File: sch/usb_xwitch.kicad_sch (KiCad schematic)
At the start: 42 parts

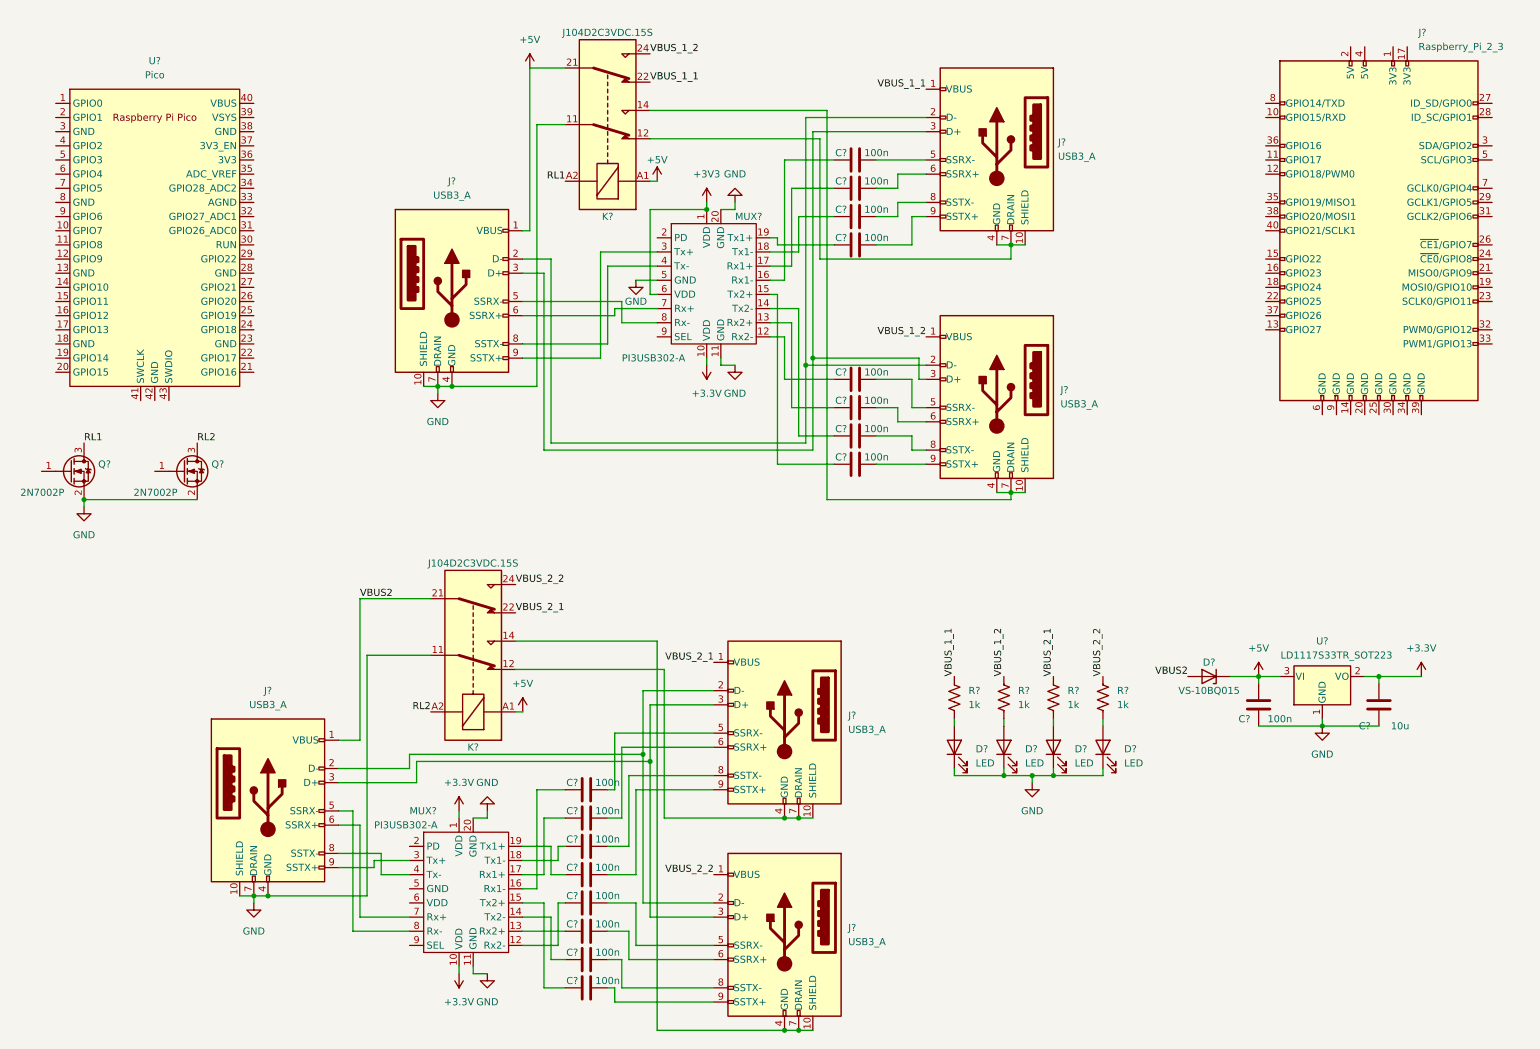
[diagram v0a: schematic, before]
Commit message: updated schematics
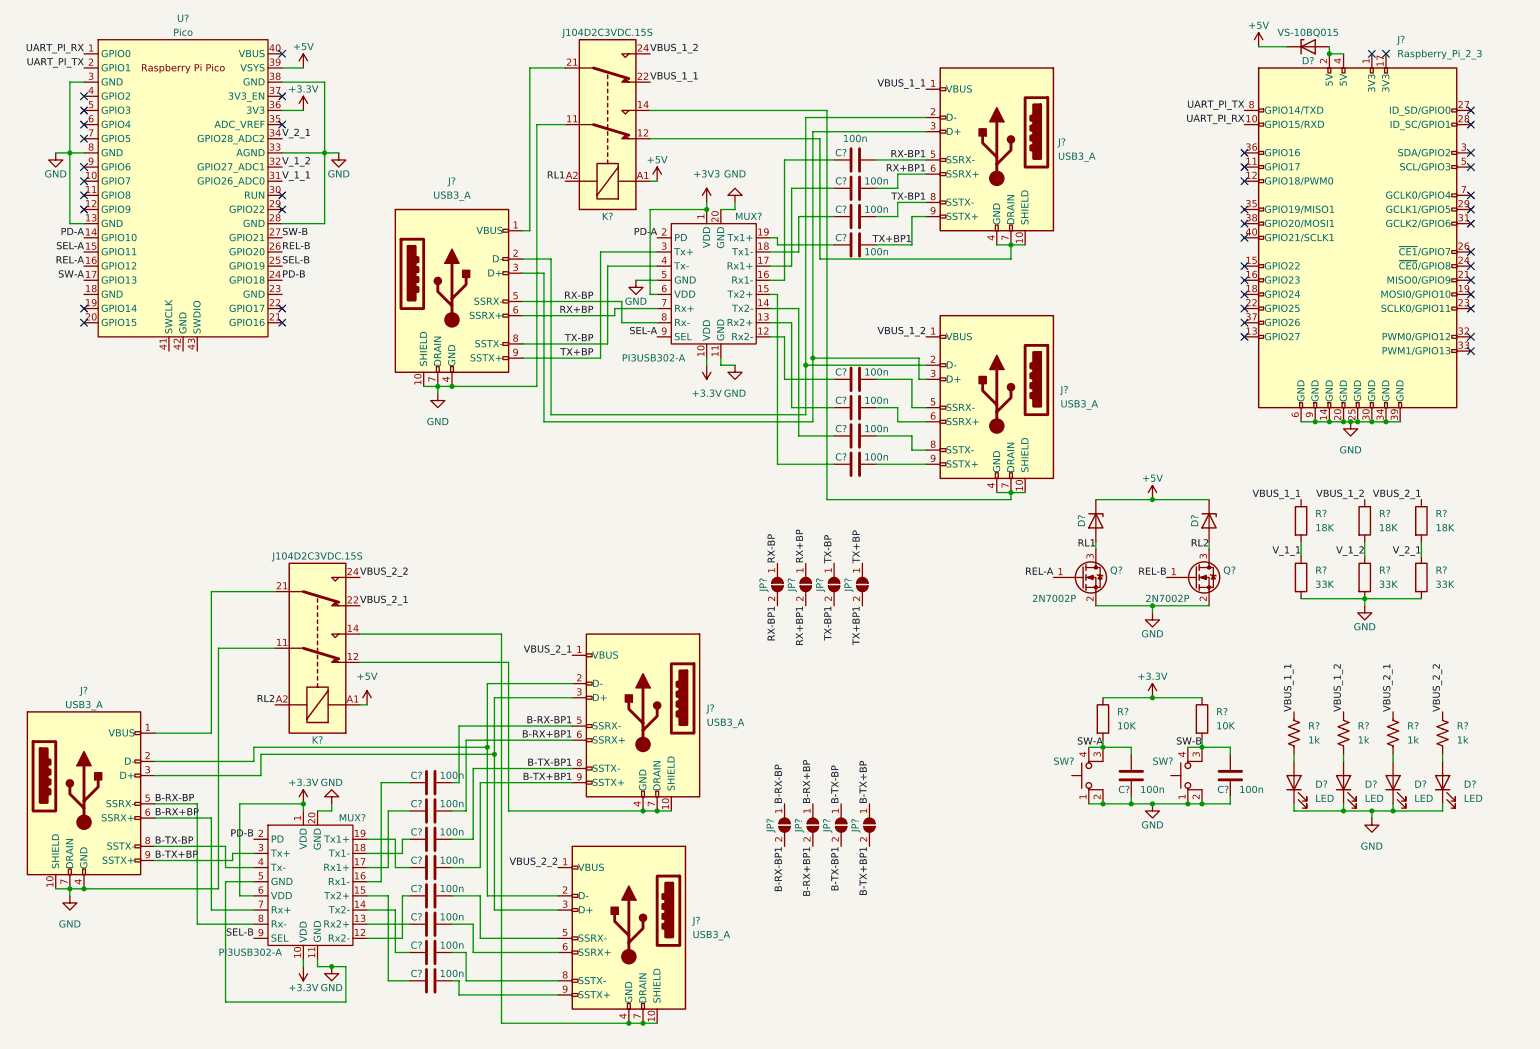
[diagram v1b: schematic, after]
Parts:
- removed C?: 10u, Capacitor_SMD:C_1206_3216Metric_Pad1.33x1.80mm_HandSolder, symbol Device:C
- removed C?: 100n, Capacitor_SMD:C_1206_3216Metric_Pad1.33x1.80mm_HandSolder, symbol Device:C
- removed D?: VS-10BQ015, Diode_SMD:D_SMB_Handsoldering, symbol Diode:Z2SMBxxx
- removed U?: LD1117S33TR_SOT223, Package_TO_SOT_SMD:SOT-223-3_TabPin2, symbol Regulator_Linear:LD1117S33TR_SOT223
- added C? (x2): 100n, Capacitor_SMD:C_1206_3216Metric_Pad1.33x1.80mm_HandSolder, symbol Device:C
- added D? (x3): VS-10BQ015, Diode_SMD:D_SMB_Handsoldering, symbol Diode:Z2SMBxxx
- added JP? (x8): SolderJumper_2_Open, Jumper:SolderJumper-2_P1.3mm_Open_RoundedPad1.0x1.5mm, symbol Jumper:SolderJumper_2_Open
- added R? (x2): 10K, Resistor_SMD:R_0603_1608Metric_Pad0.98x0.95mm_HandSolder, symbol Device:R
- added R? (x3): 18K, Resistor_SMD:R_0805_2012Metric_Pad1.20x1.40mm_HandSolder, symbol Device:R
- added R? (x3): 33K, Resistor_SMD:R_0805_2012Metric_Pad1.20x1.40mm_HandSolder, symbol Device:R
- added SW? (x2): SW_MEC_5E, symbol Switch:SW_MEC_5E
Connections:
- net +3V3: now also MUX?.6 (VDD), U?.36 (3V3), R?.1, R?.1
- net +5V: now also U?.39 (VSYS), D?.1 (K), D?.1 (K), D?.1 (K); no longer J?.1 (VBUS), K?.21
- net GND: now also J?.14 (GND), J?.20 (GND), J?.25 (GND), J?.30 (GND), J?.34 (GND), J?.39 (GND), J?.6 (GND), J?.9 (GND), MUX?.5 (GND), U?.13 (GND), U?.28 (GND), U?.3 (GND), U?.33 (AGND), U?.38 (GND), U?.8 (GND), C?.1, C?.1, R?.2, R?.2, R?.2, SW?.1, SW?.1, SW?.2, SW?.2
- net RL1: now also D?.2 (A)
- net RL2: now also D?.2 (A)
- net VBUS_1_1: now also R?.1
- net VBUS_1_2: now also R?.1
- net VBUS_2_1: now also R?.1
- net REL-A: now reaches Q?.1 (G)
- net REL-A: now also U?.16 (GPIO12)
- net B-RX-BP1: now reaches C?.2, J?.5 (SSRX-)
- net B-RX-BP1: now also JP?.2 (B)
- net B-RX+BP1: now reaches C?.2, J?.6 (SSRX+)
- net B-RX+BP1: now also JP?.2 (B)
- net B-TX-BP1: now reaches C?.2, J?.8 (SSTX-)
- net B-TX-BP1: now also JP?.2 (B)
- net B-TX+BP1: now reaches C?.2, J?.9 (SSTX+)
- net B-TX+BP1: now also JP?.2 (B)
- net PD-B: now reaches MUX?.2 (PD)
- net PD-B: now also U?.24 (GPIO18)
- net B-TX+BP: now reaches J?.9 (SSTX+), MUX?.3 (Tx+)
- net B-TX+BP: now also JP?.1 (A)
- net B-TX-BP: now reaches J?.8 (SSTX-), MUX?.4 (Tx-)
- net B-TX-BP: now also JP?.1 (A)
- net B-RX+BP: now reaches J?.6 (SSRX+), MUX?.7 (Rx+)
- net B-RX+BP: now also JP?.1 (A)
- net B-RX-BP: now reaches J?.5 (SSRX-), MUX?.8 (Rx-)
- net B-RX-BP: now also JP?.1 (A)
- net SEL-B: now reaches MUX?.9 (SEL)
- net SEL-B: now also U?.25 (GPIO19)
- net PD-A: now reaches MUX?.2 (PD)
- net PD-A: now also U?.14 (GPIO10)
- net TX+BP: now reaches J?.9 (SSTX+), MUX?.3 (Tx+)
- net TX+BP: now also JP?.1 (A)
- net TX-BP: now reaches J?.8 (SSTX-), MUX?.4 (Tx-)
- net TX-BP: now also JP?.1 (A)
- net RX+BP: now reaches J?.6 (SSRX+), MUX?.7 (Rx+)
- net RX+BP: now also JP?.1 (A)
- net RX-BP: now reaches J?.5 (SSRX-), MUX?.8 (Rx-)
- net RX-BP: now also JP?.1 (A)
- net SEL-A: now reaches MUX?.9 (SEL)
- net SEL-A: now also U?.15 (GPIO11)
- net REL-B: now reaches Q?.1 (G)
- net REL-B: now also U?.26 (GPIO20)
- net RX-BP1: now reaches C?.2, J?.5 (SSRX-)
- net RX-BP1: now also JP?.2 (B)
- net RX+BP1: now reaches C?.2, J?.6 (SSRX+)
- net RX+BP1: now also JP?.2 (B)
- net TX-BP1: now reaches C?.2, J?.8 (SSTX-)
- net TX-BP1: now also JP?.2 (B)
- net TX+BP1: now reaches C?.2, J?.9 (SSTX+)
- net TX+BP1: now also JP?.2 (B)
- net UART_PI_RX: now reaches U?.1 (GPIO0)
- net UART_PI_RX: now also J?.10 (GPIO15/RXD)
- net SW-A: now reaches U?.17 (GPIO13)
- net SW-A: now also C?.2, R?.2, SW?.3 (K), SW?.4 (A)
- net UART_PI_TX: now reaches U?.2 (GPIO1)
- net UART_PI_TX: now also J?.8 (GPIO14/TXD)
- net SW-B: now reaches U?.27 (GPIO21)
- net SW-B: now also C?.2, R?.2, SW?.3 (K), SW?.4 (A)
- net V_1_1: now reaches U?.31 (GPIO26_ADC0)
- net V_1_1: now also R?.1, R?.2
- net V_1_2: now reaches U?.32 (GPIO27_ADC1)
- net V_1_2: now also R?.1, R?.2
- net V_2_1: now reaches U?.34 (GPIO28_ADC2)
- net V_2_1: now also R?.1, R?.2
- net at J?.2 (5V): now also J?.4 (5V), D?.2 (A)
- net VBUS2: no longer names the net of J?.1 (VBUS), K?.21
- new net: J?.1 (VBUS), K?.21
- no-connect marks 0 -> 45
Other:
- moved on the sheet: C?, D?, J?, K?, MUX?, Q?, R?, U?

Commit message: add tp; ERC check
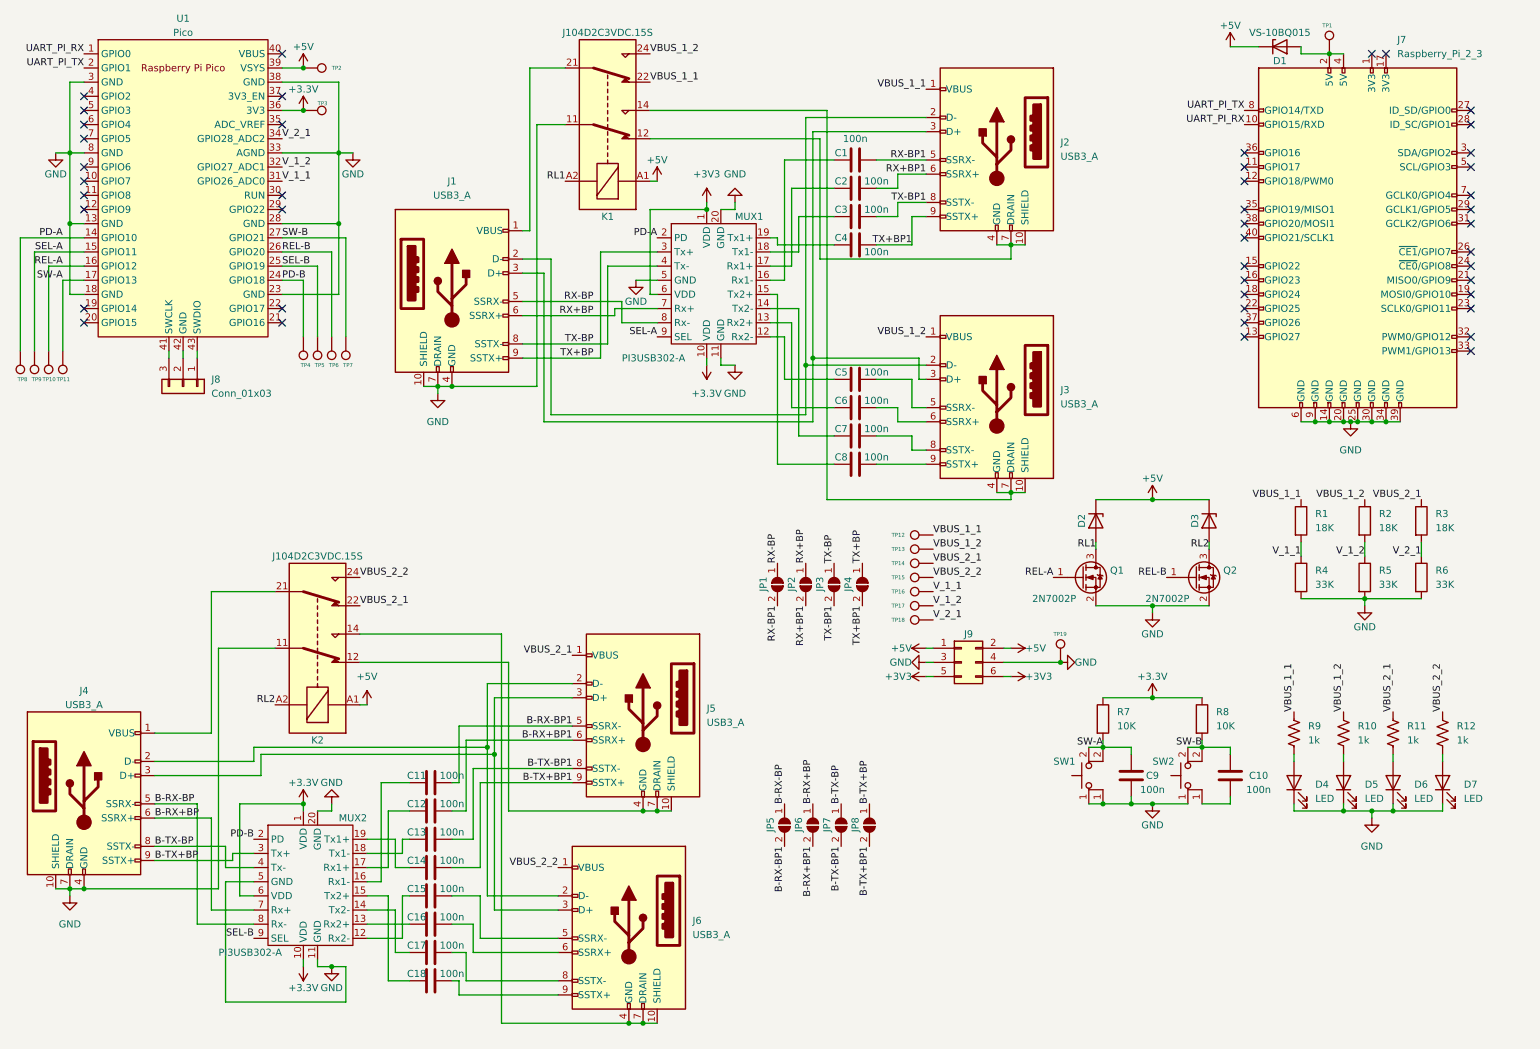
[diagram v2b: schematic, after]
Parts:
- removed SW?: SW_MEC_5E, symbol Switch:SW_MEC_5E
- added J8: Conn_01x03, Connector_PinHeader_2.00mm:PinHeader_1x03_P2.00mm_Vertical, symbol Connector_Generic:Conn_01x03
- added J9: Conn_02x03_Odd_Even, Connector_PinHeader_2.00mm:PinHeader_2x03_P2.00mm_Vertical, symbol Connector_Generic:Conn_02x03_Odd_Even
- added SW2: SW_MEC_5E, Button_Switch_THT:SW_PUSH-12mm, symbol Switch:SW_MEC_5E
- added TP1, TP10, TP11, TP12, TP13, TP14, TP15, TP16, TP17, TP18, TP19, TP2, TP3, TP4, TP5, TP6, TP7, TP8, TP9: TestPoint, TestPoint:TestPoint_Pad_D1.5mm, symbol Connector:TestPoint
- SW1: renamed from SW?; footprint (none) -> Button_Switch_THT:SW_PUSH-12mm
- gave numbers to parts that had none: 59
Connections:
- net +3V3: now also J9.5 (Pin_5), J9.6 (Pin_6), TP3.1
- net +5V: now also J9.1 (Pin_1), J9.2 (Pin_2), TP2.1
- net GND: now also U1.18 (GND), U1.23 (GND), J9.3 (Pin_3), J9.4 (Pin_4), SW2.1, TP19.1; no longer C10.1, SW1.2
- net PD-A: now also TP8.1
- net PD-B: now also TP4.1
- net REL-A: now also TP10.1
- net REL-B: now also TP6.1
- net SEL-A: now also TP9.1
- net SEL-B: now also TP5.1
- net SW-A: now also SW1.2, TP11.1; no longer SW1.3 (K), SW1.4 (A)
- net SW-B: now also SW2.2, TP7.1
- net VBUS_1_1: now also TP12.1
- net VBUS_1_2: now also TP13.1
- net VBUS_2_1: now also TP14.1
- net VBUS_2_2: now also TP15.1
- net V_1_1: now also TP16.1
- net V_1_2: now also TP17.1
- net V_2_1: now also TP18.1
- net at D1.2 (A), J7.2 (5V), J7.4 (5V): now also TP1.1
- net at U1.41 (SWCLK): now also J8.3 (Pin_3)
- net at U1.42 (GND): now also J8.2 (Pin_2)
- net at U1.43 (SWDIO): now also J8.1 (Pin_1)
- new net: C10.1, SW2.1
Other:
- moved on the sheet: D1

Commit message: updated lib using those in this repo
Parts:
- J1, J2, J3, J4, J5, J6: footprint USB3_A_AdamTech_USB-A3-S-RA:USB3_A_AdamTech_USB-A3-S-RA -> usb_xwitch:USB3_A_AdamTech_USB-A3-S-RA
- K1, K2: footprint Relay_THT:Relay_DPDT_Finder_30.22 -> usb_xwitch:J104D2C3VDC.15S
- MUX1, MUX2: symbol USB_MUX_DEMUX_PI3USB302-A:PI3USB302-A -> usb_xwitch:PI3USB302-A
- U1: symbol MCU_RaspberryPi_and_Boards:Pico -> usb_xwitch:Pico
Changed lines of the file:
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@@
     (property "Reference" "K2" (id 0) (at 67.31 143.51 90))
     (property "Value" "J104D2C3VDC.15S" (id 1) (at 67.31 110.49 90))
-    (property "Footprint" "Relay_THT:Relay_DPDT_Finder_30.22" (id 2) (at 66.548 92.71 0)
+    (property "Footprint" "usb_xwitch:J104D2C3VDC.15S" (id 2) (at 66.548 92.71 0)
       (effects (font (size 1.27 1.27)) hide)
     )
@@
       (effects (font (size 1.27 1.27)) (justify right))
     )
-    (property "Footprint" "USB3_A_AdamTech_USB-A3-S-RA:USB3_A_AdamTech_USB-A3-S-RA" (id 2) (at 185.42 78.74 0)
+    (property "Footprint" "usb_xwitch:USB3_A_AdamTech_USB-A3-S-RA" (id 2) (at 185.42 78.74 0)
       (effects (font (size 1.27 1.27)) hide)
     )
@@
       (effects (font (size 1.27 1.27)) (justify right))
     )
-    (property "Footprint" "USB3_A_AdamTech_USB-A3-S-RA:USB3_A_AdamTech_USB-A3-S-RA" (id 2) (at 121.92 135.89 0)
+    (property "Footprint" "usb_xwitch:USB3_A_AdamTech_USB-A3-S-RA" (id 2) (at 121.92 135.89 0)
       (effects (font (size 1.27 1.27)) hide)
     )
@@
     (pin "9")
   )
-  (symbol (lib_id "USB_MUX_DEMUX_PI3USB302-A:PI3USB302-A") (at 66.04 170.18 0) (unit 1)
+  (symbol (lib_id "usb_xwitch:PI3USB302-A") (at 66.04 170.18 0) (unit 1)
     (in_bom yes) (on_board yes)
     (property "Reference" "MUX2" (id 0) (at 71.12 157.48 0)
@@
     (pin "1")
   )
-  (symbol (lib_id "USB_MUX_DEMUX_PI3USB302-A:PI3USB302-A") (at 138.43 62.23 0) (unit 1)
+  (symbol (lib_id "usb_xwitch:PI3USB302-A") (at 138.43 62.23 0) (unit 1)
     (in_bom yes) (on_board yes)
     (property "Reference" "MUX1" (id 0) (at 142.24 49.53 0)
@@
       (effects (font (size 1.27 1.27)) (justify right))
     )
-    (property "Footprint" "USB3_A_AdamTech_USB-A3-S-RA:USB3_A_AdamTech_USB-A3-S-RA" (id 2) (at 119.38 173.99 0)
+    (property "Footprint" "usb_xwitch:USB3_A_AdamTech_USB-A3-S-RA" (id 2) (at 119.38 173.99 0)
       (effects (font (size 1.27 1.27)) hide)
     )
@@
     (property "Reference" "J4" (id 0) (at 25.4 134.62 0))
     (property "Value" "USB3_A" (id 1) (at 25.4 137.16 0))
-    (property "Footprint" "USB3_A_AdamTech_USB-A3-S-RA:USB3_A_AdamTech_USB-A3-S-RA" (id 2) (at 29.21 149.86 0)
+    (property "Footprint" "usb_xwitch:USB3_A_AdamTech_USB-A3-S-RA" (id 2) (at 29.21 149.86 0)
       (effects (font (size 1.27 1.27)) hide)
     )
@@
     (property "Reference" "J1" (id 0) (at 91.44 43.18 0))
     (property "Value" "USB3_A" (id 1) (at 91.44 45.72 0))
-    (property "Footprint" "USB3_A_AdamTech_USB-A3-S-RA:USB3_A_AdamTech_USB-A3-S-RA" (id 2) (at 95.25 59.69 0)
+    (property "Footprint" "usb_xwitch:USB3_A_AdamTech_USB-A3-S-RA" (id 2) (at 95.25 59.69 0)
       (effects (font (size 1.27 1.27)) hide)
     )
@@
       (effects (font (size 1.27 1.27)) (justify right))
     )
-    (property "Footprint" "USB3_A_AdamTech_USB-A3-S-RA:USB3_A_AdamTech_USB-A3-S-RA" (id 2) (at 185.42 34.29 0)
+    (property "Footprint" "usb_xwitch:USB3_A_AdamTech_USB-A3-S-RA" (id 2) (at 185.42 34.29 0)
       (effects (font (size 1.27 1.27)) hide)
     )
@@
     (property "Reference" "K1" (id 0) (at 119.38 49.53 90))
     (property "Value" "J104D2C3VDC.15S" (id 1) (at 119.38 16.51 90))
-    (property "Footprint" "Relay_THT:Relay_DPDT_Finder_30.22" (id 2) (at 118.618 -1.27 0)
+    (property "Footprint" "usb_xwitch:J104D2C3VDC.15S" (id 2) (at 118.618 -1.27 0)
       (effects (font (size 1.27 1.27)) hide)
     )
@@
     (pin "1")
   )
-  (symbol (lib_id "MCU_RaspberryPi_and_Boards:Pico") (at 43.18 44.45 0) (unit 1)
+  (symbol (lib_id "usb_xwitch:Pico") (at 43.18 44.45 0) (unit 1)
     (in_bom yes) (on_board yes)
     (property "Reference" "U1" (id 0) (at 43.18 13.97 0))
@@
     )
     (path "/8631f63c-abc2-47db-96b3-ee2fd07e9d0a"
-      (reference "J1") (unit 1) (value "USB3_A") (footprint "USB3_A_AdamTech_USB-A3-S-RA:USB3_A_AdamTech_USB-A3-S-RA")
+      (reference "J1") (unit 1) (value "USB3_A") (footprint "usb_xwitch:USB3_A_AdamTech_USB-A3-S-RA")
     )
     (path "/9118b6c6-d9a2-47dd-aea5-27a2b79677e2"
-      (reference "J2") (unit 1) (value "USB3_A") (footprint "USB3_A_AdamTech_USB-A3-S-RA:USB3_A_AdamTech_USB-A3-S-RA")
+      (reference "J2") (unit 1) (value "USB3_A") (footprint "usb_xwitch:USB3_A_AdamTech_USB-A3-S-RA")
     )
     (path "/17ca6d2b-651b-475e-9133-2f1f98ecc630"
-      (reference "J3") (unit 1) (value "USB3_A") (footprint "USB3_A_AdamTech_USB-A3-S-RA:USB3_A_AdamTech_USB-A3-S-RA")
+      (reference "J3") (unit 1) (value "USB3_A") (footprint "usb_xwitch:USB3_A_AdamTech_USB-A3-S-RA")
     )
     (path "/7777c39f-7409-4ac6-aa45-921399788f7d"
-      (reference "J4") (unit 1) (value "USB3_A") (footprint "USB3_A_AdamTech_USB-A3-S-RA:USB3_A_AdamTech_USB-A3-S-RA")
+      (reference "J4") (unit 1) (value "USB3_A") (footprint "usb_xwitch:USB3_A_AdamTech_USB-A3-S-RA")
     )
     (path "/32613975-ea2d-458f-a092-8f2ed600fa0e"
-      (reference "J5") (unit 1) (value "USB3_A") (footprint "USB3_A_AdamTech_USB-A3-S-RA:USB3_A_AdamTech_USB-A3-S-RA")
+      (reference "J5") (unit 1) (value "USB3_A") (footprint "usb_xwitch:USB3_A_AdamTech_USB-A3-S-RA")
     )
     (path "/734cb3cf-5e33-4360-8951-f60daf4bf50c"
-      (reference "J6") (unit 1) (value "USB3_A") (footprint "USB3_A_AdamTech_USB-A3-S-RA:USB3_A_AdamTech_USB-A3-S-RA")
+      (reference "J6") (unit 1) (value "USB3_A") (footprint "usb_xwitch:USB3_A_AdamTech_USB-A3-S-RA")
     )
     (path "/eeb933f2-c08b-4d89-bcac-799c4990513e"
@@
     )
     (path "/a781a132-2044-4d8e-a231-2f6e7cadcd25"
-      (reference "K1") (unit 1) (value "J104D2C3VDC.15S") (footprint "Relay_THT:Relay_DPDT_Finder_30.22")
+      (reference "K1") (unit 1) (value "J104D2C3VDC.15S") (footprint "usb_xwitch:J104D2C3VDC.15S")
     )
     (path "/0736d952-e7d6-49f7-9fe4-a9d4b55253bf"
-      (reference "K2") (unit 1) (value "J104D2C3VDC.15S") (footprint "Relay_THT:Relay_DPDT_Finder_30.22")
+      (reference "K2") (unit 1) (value "J104D2C3VDC.15S") (footprint "usb_xwitch:J104D2C3VDC.15S")
     )
     (path "/591ecbed-217e-48ed-ad79-2bef374432df"
